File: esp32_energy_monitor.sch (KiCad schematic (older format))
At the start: 60 parts, among them IC1 CP2102N-A01-GQFN28, IC2 TPS63031DSKT, IC3 MCP73830T-2AAI_MYY, J1 USB_OTG, J2 Conn_01x03, J3 Conn_01x02, J5 Conn_01x02, Q1 SS8050-G, Q2 SS8050-G, Q3 CSD16406Q3, Q4 CSD16406Q3, SW1 SW_Push, SW2 SW_Push, U2 BQ29700DSET

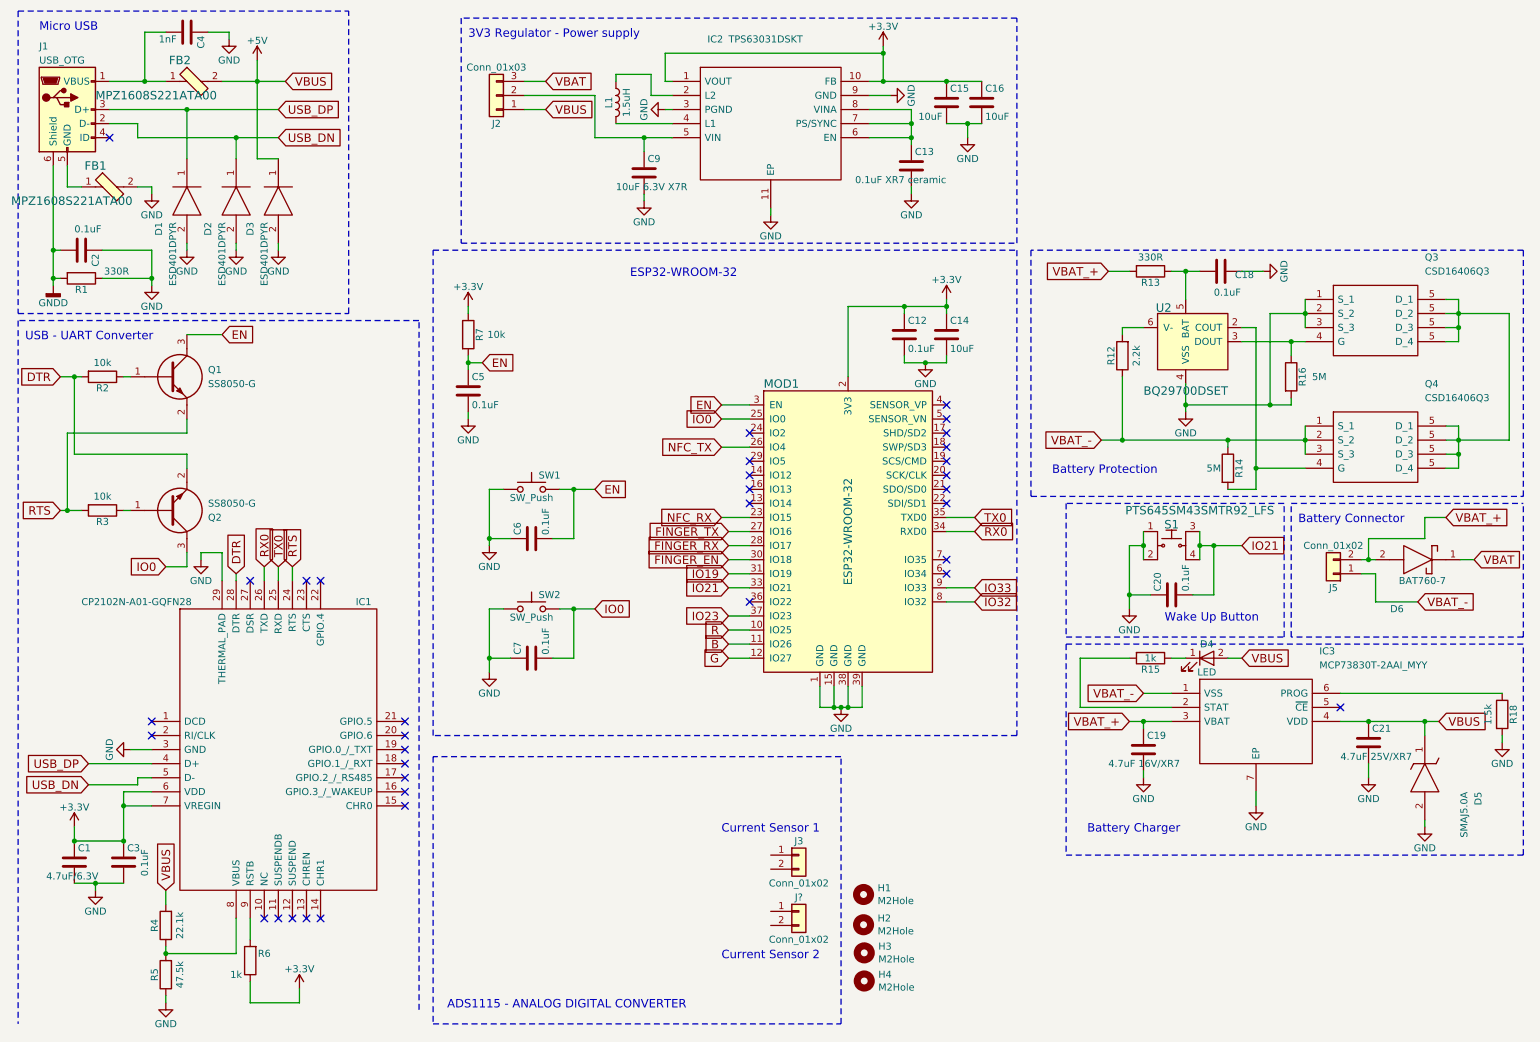
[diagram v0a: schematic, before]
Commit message: Added the ADS1115IDGSR ADC circuit with the signal conditioning to current sensor SCT-013-020 (30A).
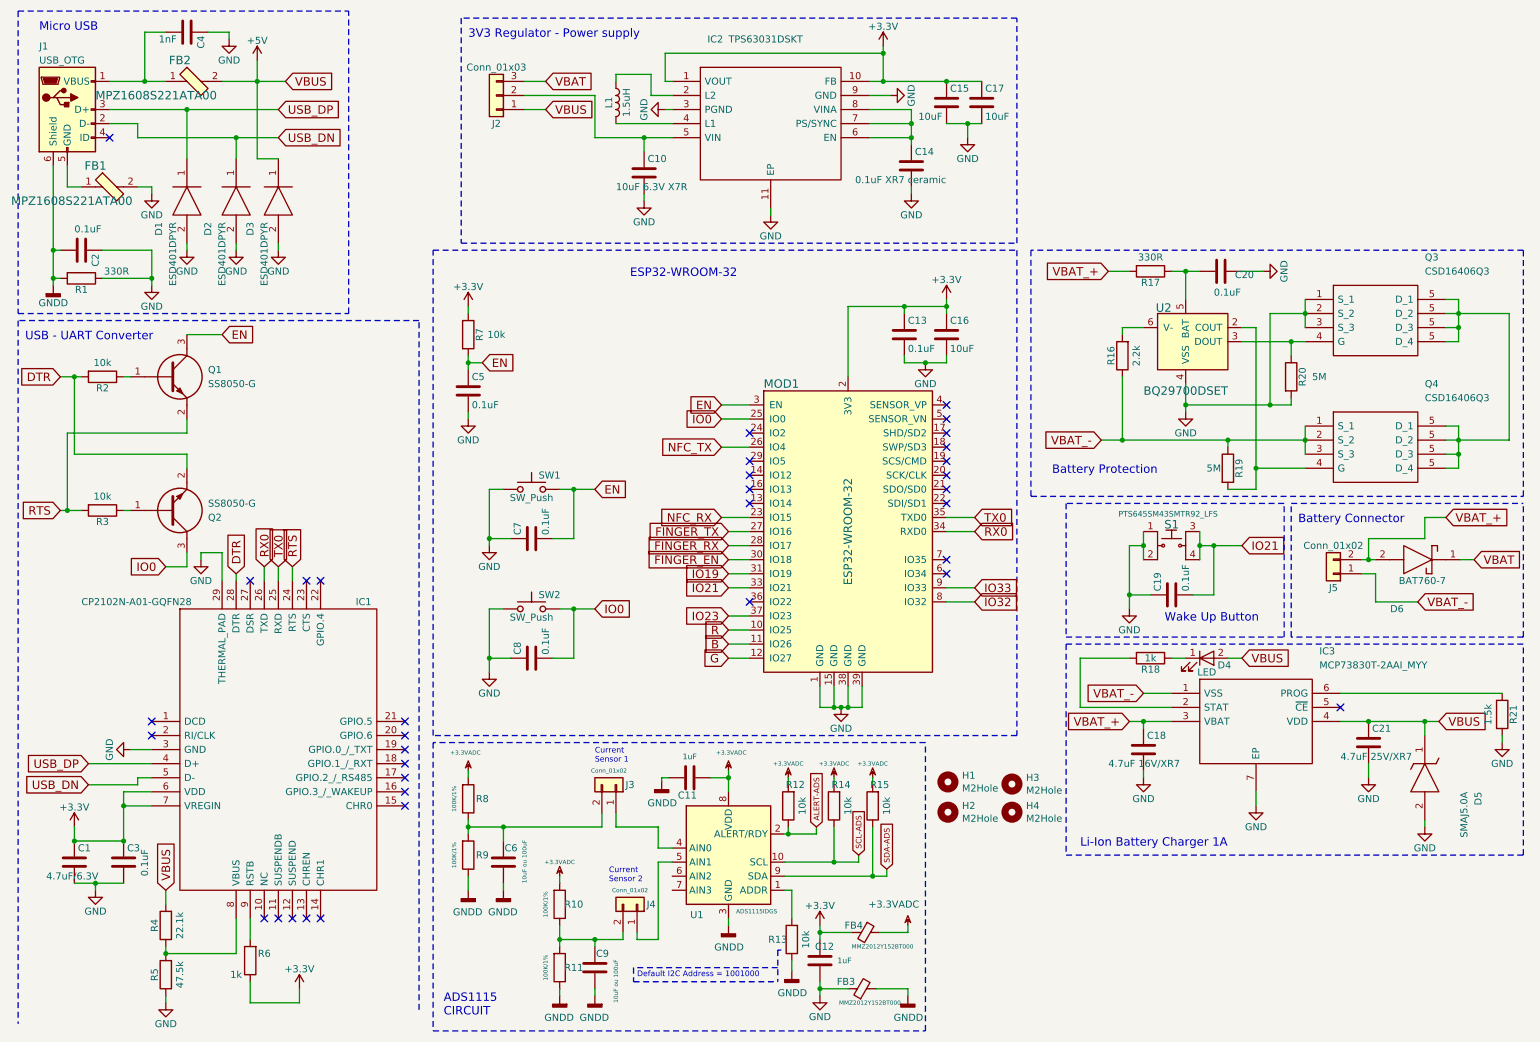
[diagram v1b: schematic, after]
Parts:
- added C11, C12: 1uF, Capacitors_SMD:C_0603, symbol esp32_energy_monitor-rescue:C-padlock-rescue
- added C6, C9: 10uF ou 100uF, Capacitors_SMD:C_0603, symbol esp32_energy_monitor-rescue:C-padlock-rescue
- added FB3, FB4: MMZ2012Y152BT000, Inductor_SMD:L_0805_2012Metric, symbol Device:Ferrite_Bead_Small
- added R10, R11, R8, R9: 100K/1%, Resistors_SMD:R_0603, symbol esp32_energy_monitor-rescue:R-padlock-rescue
- added R12, R13, R14, R15: 10k, Resistors_SMD:R_0603, symbol esp32_energy_monitor-rescue:R-padlock-rescue
- added U1: ADS1115IDGS, Package_SO:TSSOP-10_3x3mm_P0.5mm, symbol Analog_ADC:ADS1115IDGS
- gave numbers to parts that had none: 1
- renumbered C9 to C10, C12 to C13, C13 to C14, C14 to C16, C16 to C17, C19 to C18, C20 to C19, C18 to C20, C6 to C7, C7 to C8, R12 to R16, R13 to R17, R15 to R18, R14 to R19, R16 to R20, R18 to R21
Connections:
- net +3V3: now also C12.1, FB4.2
- net GND: now also C12.2, FB3.1
- net GNDD: now also C11.1, C6.2, C9.2, FB3.2, R11.1, R13.1, R9.1, U1.3 (GND)
- net at J3.1 (Pin_1): now also U1.4 (AIN0)
- net at J3.2 (Pin_2): now also C6.1, R8.1, R9.2
- net at J4.1 (Pin_1): now also U1.5 (AIN1)
- net at J4.2 (Pin_2): now also C9.1, R10.1, R11.2
- new net: R13.2, U1.1 (ADDR)
- new net +3.3VADC: C11.2, FB4.1, R10.2, R12.2, R14.2, R15.2, R8.2, U1.8 (VDD)
- new net ALERT-ADS: R12.1, U1.2 (ALERT/RDY)
- new net SCL-ADS: R14.1, U1.10 (SCL)
- new net SDA-ADS: R15.1, U1.9 (SDA)
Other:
- note added: "ADS1115\nCIRCUIT"
- note added: "Current \nSensor 1"
- note added: "Current \nSensor 2"
- note added: "Default I2C Address = 1001000"
- note added: "Li-Ion Battery Charger 1A\n"
- note removed: "ADS1115 - ANALOG DIGITAL CONVERTER"
- note removed: "Battery Charger"
- note removed: "Current Sensor 1"
- note removed: "Current Sensor 2"
- moved on the sheet: H1, H2, H3, H4, J3, J4

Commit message: Schematic: Removed ADS1115 circuit. Removed Battery Protection circuit. Removed Battery Charger circuit. Removed Wake Up Button. Added external access circuit. Added three current measure circuit. It will be powered with power supply micro-usb only.
Layout:
Added the footprint library of the project.
Changed the ESP32 footprint.
Changed the position of the power supply circuit. (near of USB connector)

3D View:
Added ESP32 3D format step.
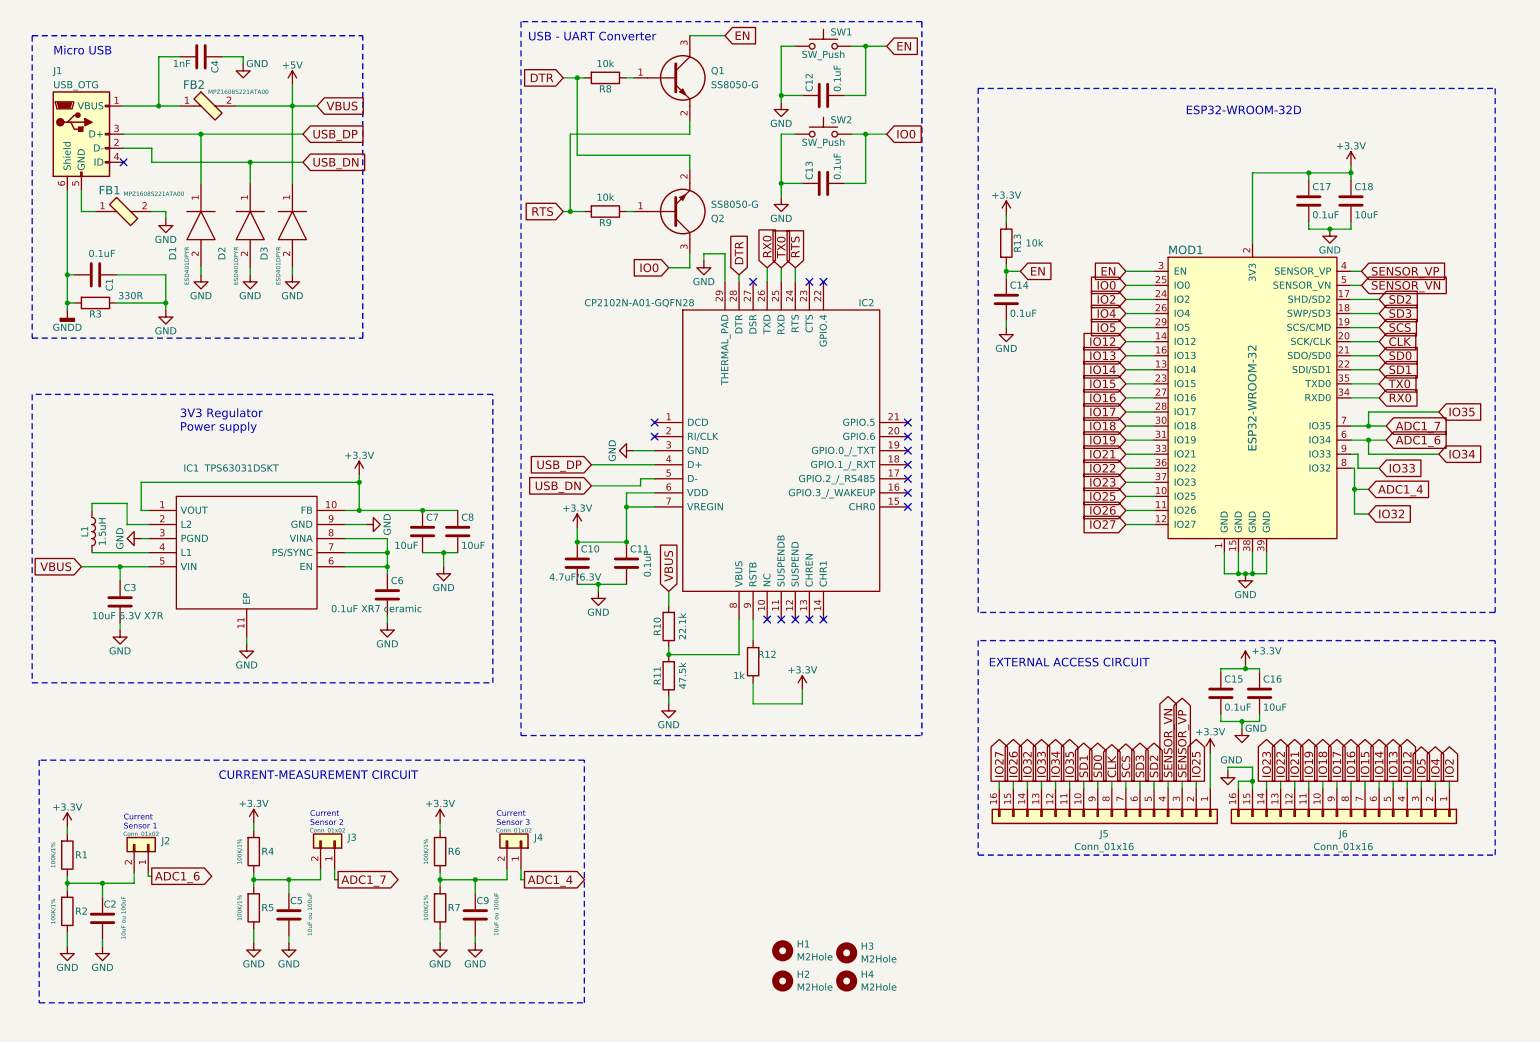
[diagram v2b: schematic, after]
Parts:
- removed C11, C12: 1uF, Capacitors_SMD:C_0603, symbol esp32_energy_monitor-rescue:C-padlock-rescue
- removed C18: 4.7uF 16V/XR7, Capacitors_SMD:C_0805, symbol esp32_energy_monitor-rescue:C-padlock-rescue
- removed C19, C20: 0.1uF, Capacitors_SMD:C_0603, symbol esp32_energy_monitor-rescue:C-padlock-rescue
- removed C21: 4.7uF 25V/XR7, Capacitors_SMD:C_1206, symbol esp32_energy_monitor-rescue:C-padlock-rescue
- removed D4: LED, LEDs:LED_0603, symbol esp32_energy_monitor-rescue:LED-padlock-rescue
- removed D5: SMAJ5.0A, SamacSys_Parts:DIOM5026X229N, symbol esp32_energy_monitor-rescue:SMAJ5.0A-padlock-rescue
- removed D6: BAT760-7, SamacSys_Parts:SOD2513X120N, symbol esp32_energy_monitor-rescue:BAT760-7-padlock-rescue
- removed FB3, FB4: MMZ2012Y152BT000, Inductor_SMD:L_0805_2012Metric, symbol Device:Ferrite_Bead_Small
- removed IC3: MCP73830T-2AAI_MYY, SamacSys_Parts:SON50P200X200X80-7N-D, symbol esp32_energy_monitor-rescue:MCP73830T-2AAI_MYY-padlock-rescue
- removed J2: Conn_01x03, Pin_Headers:Pin_Header_Straight_1x03_Pitch2.54mm, symbol esp32_energy_monitor-rescue:Conn_01x03-padlock-rescue
- removed J5: Conn_01x02, Pin_Headers:Pin_Header_Straight_1x02_Pitch2.54mm, symbol esp32_energy_monitor-rescue:Conn_01x02-padlock-rescue
- removed Q3, Q4: CSD16406Q3, SamacSys_Parts:DQG_VSON-CLIP, symbol esp32_energy_monitor-rescue:CSD16406Q3-padlock-rescue
- removed R10, R11: 100K/1%, Resistors_SMD:R_0603, symbol esp32_energy_monitor-rescue:R-padlock-rescue
- removed R12, R13, R14, R15: 10k, Resistors_SMD:R_0603, symbol esp32_energy_monitor-rescue:R-padlock-rescue
- removed R16: 2.2k, Resistors_SMD:R_0603, symbol esp32_energy_monitor-rescue:R-padlock-rescue
- removed R17: 330R, Resistors_SMD:R_0603, symbol esp32_energy_monitor-rescue:R-padlock-rescue
- removed R18: 1k, Resistors_SMD:R_0603, symbol esp32_energy_monitor-rescue:R-padlock-rescue
- removed R19, R20: 5M, Resistors_SMD:R_0603, symbol esp32_energy_monitor-rescue:R-padlock-rescue
- removed R21: 1.5k, Resistors_SMD:R_0603, symbol esp32_energy_monitor-rescue:R-padlock-rescue
- removed S1: PTS645SM43SMTR92_LFS, digikey-footprints:Switch_Tactile_SMD_6x6mm_PTS645, symbol esp32_energy_monitor-rescue:PTS645SM43SMTR92_LFS-padlock-rescue
- removed U1: ADS1115IDGS, Package_SO:TSSOP-10_3x3mm_P0.5mm, symbol Analog_ADC:ADS1115IDGS
- removed U2: BQ29700DSET, SamacSys_Parts:SON50P150X150X80-6N, symbol esp32_energy_monitor-rescue:BQ29700DSET-padlock-rescue
- added C15: 0.1uF, proj_kicad_esp32_energy_consumption:C_0603, symbol esp32_energy_monitor-rescue:C-padlock-rescue
- added C16: 10uF, proj_kicad_esp32_energy_consumption:C_0603, symbol esp32_energy_monitor-rescue:C-padlock-rescue
- added C2: 10uF ou 100uF, proj_kicad_esp32_energy_consumption:C_0603, symbol esp32_energy_monitor-rescue:C-padlock-rescue
- added J2: Conn_01x02, proj_kicad_esp32_energy_consumption:Pin_Header_Straight_1x02_Pitch2.54mm, symbol esp32_energy_monitor-rescue:Conn_01x02-padlock-rescue
- added J5, J6: Conn_01x16, Connector_PinHeader_2.54mm:PinHeader_1x16_P2.54mm_Vertical, symbol Connector_Generic:Conn_01x16
- added R1, R2, R6, R7: 100K/1%, proj_kicad_esp32_energy_consumption:R_0603, symbol esp32_energy_monitor-rescue:R-padlock-rescue
- C1: renamed from C2; footprint Capacitors_SMD:C_0603 -> proj_kicad_esp32_energy_consumption:C_0603
- C10: renamed from C1; footprint Capacitors_SMD:C_0603 -> proj_kicad_esp32_energy_consumption:C_0603
- C11: renamed from C3; footprint Capacitors_SMD:C_0603 -> proj_kicad_esp32_energy_consumption:C_0603
- C12: renamed from C7; footprint Capacitors_SMD:C_0603 -> proj_kicad_esp32_energy_consumption:C_0603
- C13: renamed from C8; footprint Capacitors_SMD:C_0603 -> proj_kicad_esp32_energy_consumption:C_0603
- C14: renamed from C5; footprint Capacitors_SMD:C_0603 -> proj_kicad_esp32_energy_consumption:C_0603
- C17: renamed from C13; footprint Capacitors_SMD:C_0603 -> proj_kicad_esp32_energy_consumption:C_0603
- C18: renamed from C16; footprint Capacitors_SMD:C_0603 -> proj_kicad_esp32_energy_consumption:C_0603
- C3: renamed from C10; footprint Capacitors_SMD:C_0603 -> proj_kicad_esp32_energy_consumption:C_0603
- C4, C9: footprint Capacitors_SMD:C_0603 -> proj_kicad_esp32_energy_consumption:C_0603
- C5: renamed from C6; footprint Capacitors_SMD:C_0603 -> proj_kicad_esp32_energy_consumption:C_0603
- C6: renamed from C14; footprint Capacitors_SMD:C_0603 -> proj_kicad_esp32_energy_consumption:C_0603
- C7: renamed from C15; footprint Capacitors_SMD:C_0603 -> proj_kicad_esp32_energy_consumption:C_0603
- C8: renamed from C17; footprint Capacitors_SMD:C_0603 -> proj_kicad_esp32_energy_consumption:C_0603
- D1, D2, D3: footprint padlock.pretty:DPY_R-PX1SON-N2_ -> proj_kicad_esp32_energy_consumption:DPY_R-PX1SON-N2_
- FB1, FB2: footprint digikey-footprints:0603 -> proj_kicad_esp32_energy_consumption:0603
- H1, H2, H3, H4: footprint Mounting_Holes:MountingHole_2.2mm_M2_DIN965 -> proj_kicad_esp32_energy_consumption:MountingHole_2.2mm_M2_DIN965
- IC1: renamed from IC2; footprint SamacSys_Parts:SON50P250X250X80-11N-D -> proj_kicad_esp32_energy_consumption:SON50P250X250X80-11N-D
- IC2: renamed from IC1; footprint SamacSys_Parts:QFN50P500X500X80-29N-D -> proj_kicad_esp32_energy_consumption:QFN50P500X500X80-29N-D
- J1: footprint digikey-footprints:USB_Micro_B_Female_1050170001 -> proj_kicad_esp32_energy_consumption:USB_Micro_B_Female_1050170001
- J3, J4: footprint Pin_Headers:Pin_Header_Straight_1x02_Pitch2.54mm -> proj_kicad_esp32_energy_consumption:Pin_Header_Straight_1x02_Pitch2.54mm
- L1: footprint SamacSys_Parts:INDC3030X120N -> proj_kicad_esp32_energy_consumption:INDC3030X120N
- MOD1: footprint padlock.pretty:ESP32-WROOM-32U -> ESP32-WROOM-32D:ESP32WROOM32D
- Q1, Q2: footprint SamacSys_Parts:SOT95P240X115-3N -> proj_kicad_esp32_energy_consumption:SOT95P240X115-3N
- R10: renamed from R4; footprint Resistors_SMD:R_0603 -> proj_kicad_esp32_energy_consumption:R_0603
- R11: renamed from R5; footprint Resistors_SMD:R_0603 -> proj_kicad_esp32_energy_consumption:R_0603
- R12: renamed from R6; footprint Resistors_SMD:R_0603 -> proj_kicad_esp32_energy_consumption:R_0603
- R13: renamed from R7; footprint Resistors_SMD:R_0603 -> proj_kicad_esp32_energy_consumption:R_0603
- R3: renamed from R1; footprint Resistors_SMD:R_0603 -> proj_kicad_esp32_energy_consumption:R_0603
- R4: renamed from R8; footprint Resistors_SMD:R_0603 -> proj_kicad_esp32_energy_consumption:R_0603
- R5: renamed from R9; footprint Resistors_SMD:R_0603 -> proj_kicad_esp32_energy_consumption:R_0603
- R8: renamed from R2; footprint Resistors_SMD:R_0603 -> proj_kicad_esp32_energy_consumption:R_0603
- R9: renamed from R3; footprint Resistors_SMD:R_0603 -> proj_kicad_esp32_energy_consumption:R_0603
- SW1, SW2: footprint Buttons_Switches_SMD:SW_SPST_B3U-1000P -> proj_kicad_esp32_energy_consumption:SW_SPST_B3U-1000P
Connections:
- net +3.3VADC is gone; now on net +3V3: R4.2
- net IO32 is gone; now on net ADC1_4: MOD1.8 (IO32)
- net +3V3: now also C15.1, C16.1, J5.1 (Pin_1), R1.2, R6.2
- net +5V: now also C3.1, IC1.5 (VIN)
- net GND: now also C5.2, C9.2, R5.1, C15.2, C16.2, C2.2, J6.15 (Pin_15), J6.16 (Pin_16), R2.1, R7.1
- net GNDD: no longer C5.2, C9.2, R5.1
- net IO19: now also J6.11 (Pin_11)
- net IO21: now also J6.12 (Pin_12)
- net IO23: now also J6.14 (Pin_14)
- net IO33: now also J5.13 (Pin_13)
- net IO14: now reaches MOD1.13 (IO14)
- net IO14: now also J6.6 (Pin_6)
- net IO12: now reaches MOD1.14 (IO12)
- net IO12: now also J6.4 (Pin_4)
- net IO13: now reaches MOD1.16 (IO13)
- net IO13: now also J6.5 (Pin_5)
- net SD2: now reaches MOD1.17 (SHD/SD2)
- net SD2: now also J5.5 (Pin_5)
- net SD3: now reaches MOD1.18 (SWP/SD3)
- net SD3: now also J5.6 (Pin_6)
- net SCS: now reaches MOD1.19 (SCS/CMD)
- net SCS: now also J5.7 (Pin_7)
- net CLK: now reaches MOD1.20 (SCK/CLK)
- net CLK: now also J5.8 (Pin_8)
- net SD0: now reaches MOD1.21 (SDO/SD0)
- net SD0: now also J5.9 (Pin_9)
- net SD1: now reaches MOD1.22 (SDI/SD1)
- net SD1: now also J5.10 (Pin_10)
- net IO2: now reaches MOD1.24 (IO2)
- net IO2: now also J6.1 (Pin_1)
- net IO5: now reaches MOD1.29 (IO5)
- net IO5: now also J6.3 (Pin_3)
- net IO22: now reaches MOD1.36 (IO22)
- net IO22: now also J6.13 (Pin_13)
- net SENSOR_VP: now reaches MOD1.4 (SENSOR_VP)
- net SENSOR_VP: now also J5.3 (Pin_3)
- net SENSOR_VN: now reaches MOD1.5 (SENSOR_VN)
- net SENSOR_VN: now also J5.4 (Pin_4)
- net ADC1_6: now reaches MOD1.6 (IO34)
- net ADC1_6: now also J2.1 (Pin_1), J5.12 (Pin_12)
- net ADC1_7: now reaches MOD1.7 (IO35)
- net ADC1_7: now also J3.1 (Pin_1), J5.11 (Pin_11)
- net ADC1_4: now reaches J4.1 (Pin_1)
- net ADC1_4: now also J5.14 (Pin_14)
- net at C9.1, J4.2 (Pin_2): now also R6.1, R7.2
- net B renamed IO26
- net IO26: now also J5.15 (Pin_15)
- net FINGER_EN renamed IO18
- net IO18: now also J6.10 (Pin_10)
- net FINGER_RX renamed IO17
- net IO17: now also J6.9 (Pin_9)
- net FINGER_TX renamed IO16
- net IO16: now also J6.8 (Pin_8)
- net G renamed IO27
- net IO27: now also J5.16 (Pin_16)
- net NFC_RX renamed IO15
- net IO15: now also J6.7 (Pin_7)
- net NFC_TX renamed IO4
- net IO4: now also J6.2 (Pin_2)
- net R renamed IO25
- net IO25: now also J5.2 (Pin_2)
- new net: C2.1, J2.2 (Pin_2), R1.1, R2.2
- no-connect marks 35 -> 18
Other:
- note added: "3V3 Regulator\nPower supply"
- note added: "CURRENT-MEASUREMENT CIRCUIT"
- note added: "Current \nSensor 3"
- note added: "ESP32-WROOM-32D"
- note added: "EXTERNAL ACCESS CIRCUIT"
- note removed: "3V3 Regulator - Power supply"
- note removed: "ADS1115\nCIRCUIT"
- note removed: "Battery Connector"
- note removed: "Battery Protection"
- note removed: "Default I2C Address = 1001000"
- note removed: "ESP32-WROOM-32"
- note removed: "Li-Ion Battery Charger 1A\n"
- note removed: "Wake Up Button"
- moved on the sheet: C1, C10, C11, C12, C13, C14, C17, C18, C3, C4, C5, C6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

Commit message: Added to the library of the project the pin header footprint. Added the first version of the Bill of the Materials (BoM) of the board. Added the StackUp of the board.
Schematic:
Changed the position of the pins on J5 and J6 to layout better on the board.

Layout:
Added all the route tracks of the J5 and J6 connectors
Added 3V3 Power Plane and the VBUS Power Plane
Changed the format of the Ground Plane.
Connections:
- net ADC1_4: now also J5.13 (Pin_13); no longer J5.14 (Pin_14)
- net IO12: now also J6.2 (Pin_2); no longer J6.4 (Pin_4)
- net IO13: now also J6.3 (Pin_3); no longer J6.5 (Pin_5)
- net IO14: now also J6.1 (Pin_1); no longer J6.6 (Pin_6)
- net IO15: now also J6.4 (Pin_4); no longer J6.7 (Pin_7)
- net IO16: now also J6.9 (Pin_9); no longer J6.8 (Pin_8)
- net IO17: now also J6.8 (Pin_8); no longer J6.9 (Pin_9)
- net IO18: now also J6.7 (Pin_7); no longer J6.10 (Pin_10)
- net IO2: now also J6.5 (Pin_5); no longer J6.1 (Pin_1)
- net IO33: now also J5.14 (Pin_14); no longer J5.13 (Pin_13)
- net IO4: now also J6.10 (Pin_10); no longer J6.2 (Pin_2)
- net IO5: now also J6.6 (Pin_6); no longer J6.3 (Pin_3)
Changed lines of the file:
@@
 NoConn ~ 6825 3925
 NoConn ~ 6825 4025
-NoConn ~ 5025 3425
-NoConn ~ 5025 3525
 NoConn ~ 6225 2425
 NoConn ~ 5925 4825
@@
 	5025 4025 4825 4025
 Connection ~ 4825 4025
-Wire Wire Line
-	5025 3725 4575 3725
 Wire Wire Line
 	4575 3875 4925 3875
@@
 Wire Wire Line
 	9975 2450 10050 2450
+Text GLabel 10275 5975 1    60   Output ~ 0
+IO2
+Text GLabel 9775 5975 1    60   Output ~ 0
+IO4
+Text GLabel 10575 5975 1    60   Output ~ 0
+IO12
+Text GLabel 10475 5975 1    60   Output ~ 0
+IO13
 Text GLabel 10675 5975 1    60   Output ~ 0
-IO2
-Text GLabel 10575 5975 1    60   Output ~ 0
-IO4
-Text GLabel 10475 5975 1    60   Output ~ 0
-IO5
+IO14
 Text GLabel 10375 5975 1    60   Output ~ 0
-IO12
-Text GLabel 10275 5975 1    60   Output ~ 0
-IO13
-Text GLabel 10175 5975 1    60   Output ~ 0
-IO14
-Text GLabel 10075 5975 1    60   Output ~ 0
 IO15
 Text GLabel 9975 5975 1    60   Output ~ 0
-IO16
-Text GLabel 9875 5975 1    60   Output ~ 0
 IO17
-Text GLabel 9775 5975 1    60   Output ~ 0
+Text GLabel 10075 5975 1    60   Output ~ 0
 IO18
 Text GLabel 9675 5975 1    60   Output ~ 0
@@
 Wire Wire Line
 	2450 1175 2450 1725
+Text GLabel 7775 5975 1    60   Output ~ 0
+IO32
 Text GLabel 7675 5975 1    60   Output ~ 0
-IO32
-Text GLabel 7775 5975 1    60   Output ~ 0
 IO33
 Text GLabel 7875 5975 1    60   Output ~ 0
@@
 Text Notes 7400 5175 0    60   ~ 0
 EXTERNAL ACCESS CIRCUIT
+Text GLabel 10175 5975 1    60   Output ~ 0
+IO5
+Text GLabel 9875 5975 1    60   Output ~ 0
+IO16
+Wire Wire Line
+	5025 3725 4575 3725
+NoConn ~ 5025 3425
+NoConn ~ 5025 3525
 $EndSCHEMATC
